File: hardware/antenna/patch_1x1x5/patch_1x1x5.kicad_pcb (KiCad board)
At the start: 2 copper layers, 31.5 x 100.1 mm, 1 part

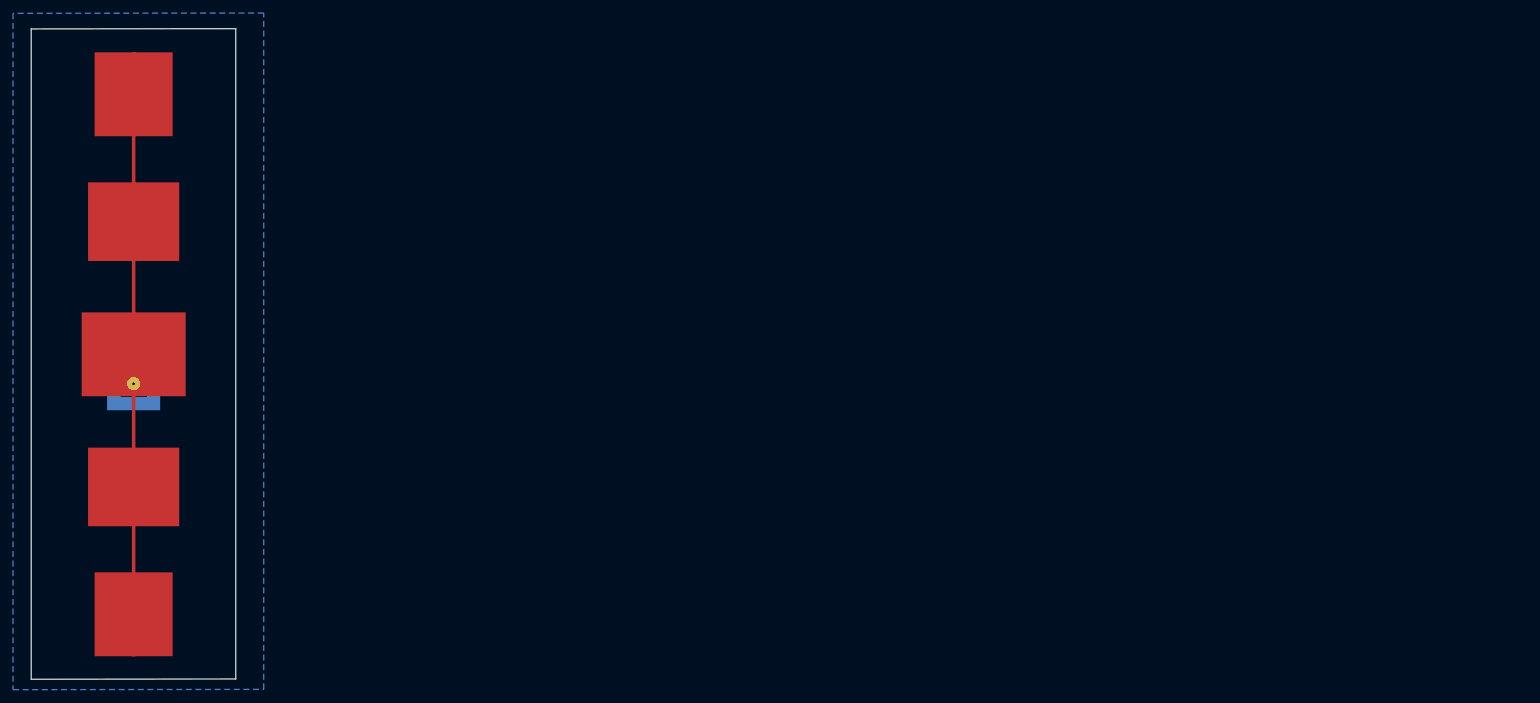
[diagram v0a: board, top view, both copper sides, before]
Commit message: Huge, messy commit before I begin replacing FPGA code
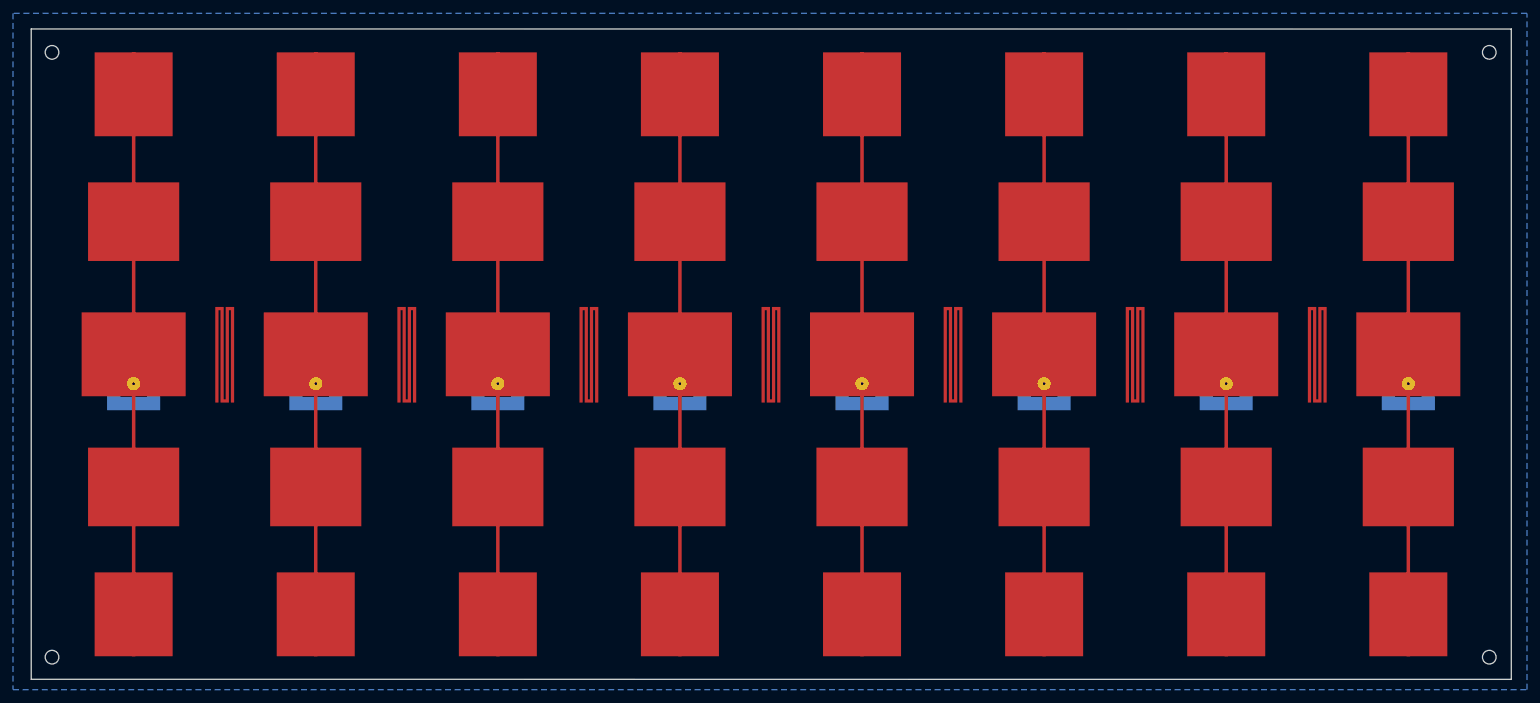
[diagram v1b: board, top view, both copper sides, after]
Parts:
- added AE1: Antenna_Chip, antennas:patch_1x5, F.Cu at (53.5, 112.0)
- added AE3: Antenna_Chip, antennas:patch_1x5, F.Cu at (109.5, 112.0)
- added AE4: Antenna_Chip, antennas:patch_1x5, F.Cu at (137.6, 112.0)
- added AE5: Antenna_Chip, antennas:patch_1x5, F.Cu at (165.6, 112.0)
- added AE6: Antenna_Chip, antennas:patch_1x5, F.Cu at (193.6, 112.0)
- added AE7: Antenna_Chip, antennas:patch_1x5, F.Cu at (221.6, 112.0)
- added AE8: Antenna_Chip, antennas:patch_1x5, F.Cu at (249.6, 112.0)
- added REF**: MountingHole_2.1mm, MountingHole:MountingHole_2.1mm, F.Cu at (262.0, 61.0)
- added REF**: patch_sep, antennas:patch_sep, F.Cu at (95.5, 107.5)
- added REF**: patch_sep, antennas:patch_sep, F.Cu at (67.5, 107.5)
- added REF**: MountingHole_2.1mm, MountingHole:MountingHole_2.1mm, F.Cu at (262.0, 154.0)
- added REF**: MountingHole_2.1mm, MountingHole:MountingHole_2.1mm, F.Cu at (41.0, 154.0)
- added REF**: MountingHole_2.1mm, MountingHole:MountingHole_2.1mm, F.Cu at (41.0, 61.0)
- added REF**: patch_sep, antennas:patch_sep, F.Cu at (235.6, 107.5)
- added REF**: patch_sep, antennas:patch_sep, F.Cu at (207.6, 107.5)
- added REF**: patch_sep, antennas:patch_sep, F.Cu at (179.6, 107.5)
- added REF**: patch_sep, antennas:patch_sep, F.Cu at (151.6, 107.5)
- added REF**: patch_sep, antennas:patch_sep, F.Cu at (123.5, 107.5)
- moved AE2 28.0 mm to (81.5, 112.0)
- renumbered AE1 to AE2
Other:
- board size 31.5 x 100.1 mm -> 227.6 x 100 mm
